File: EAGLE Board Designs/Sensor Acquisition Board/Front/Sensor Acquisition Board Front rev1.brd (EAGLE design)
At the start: 116.8 x 50.8 mm, 41 parts, among them J1 CONNECTOR-SENSOR_NF_S_RA_BLACK, J10 JUMPER_0603_, J2 CONNECTOR-SENSOR_NF_S_RA_BLACK, J3 CONNECTOR-CAN_NF_S_RA_BLACK, J4 CONNECTOR-CAN_NF_S_RA_BLACK, J6 JUMPER_0603_, U1 VOLTAGE_REGULATOR_SOT-223_5V, U2 MCP2562FD, U3 MCP2562FD

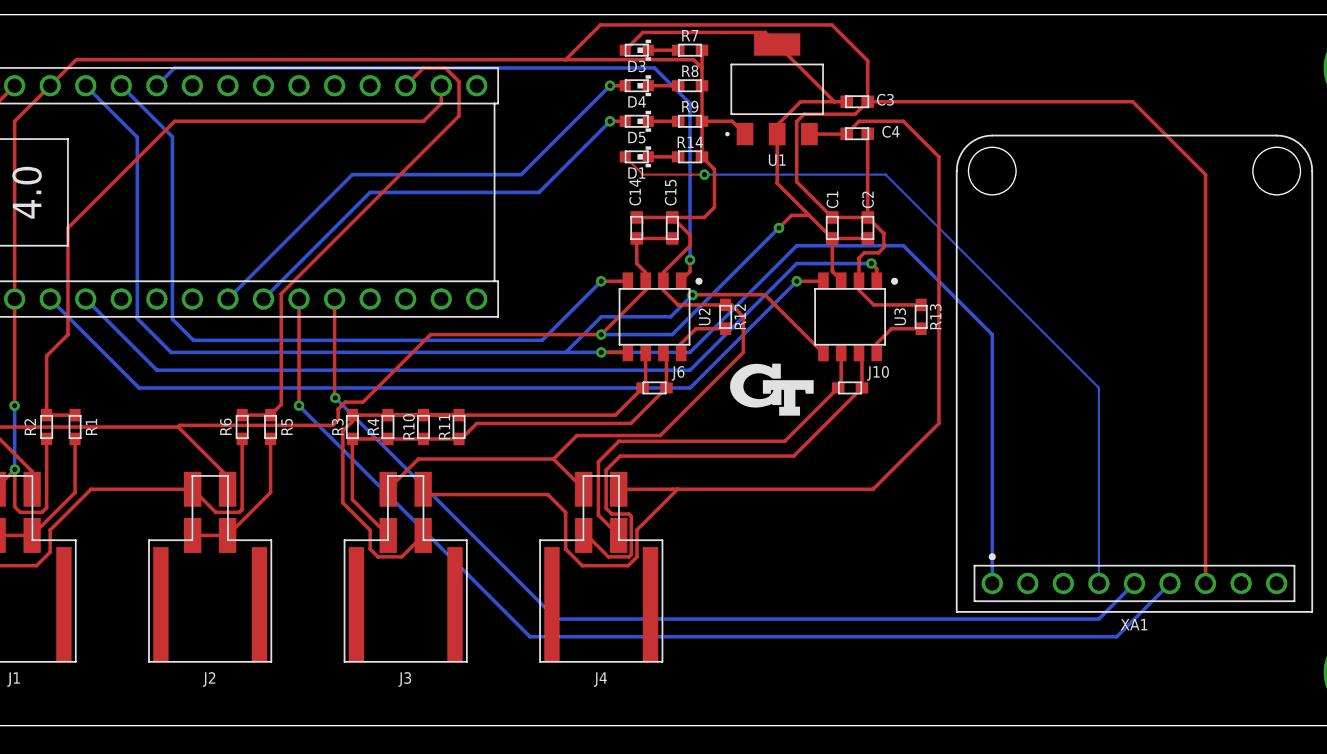
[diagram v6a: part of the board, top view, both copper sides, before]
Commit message: Fixed GPS connections
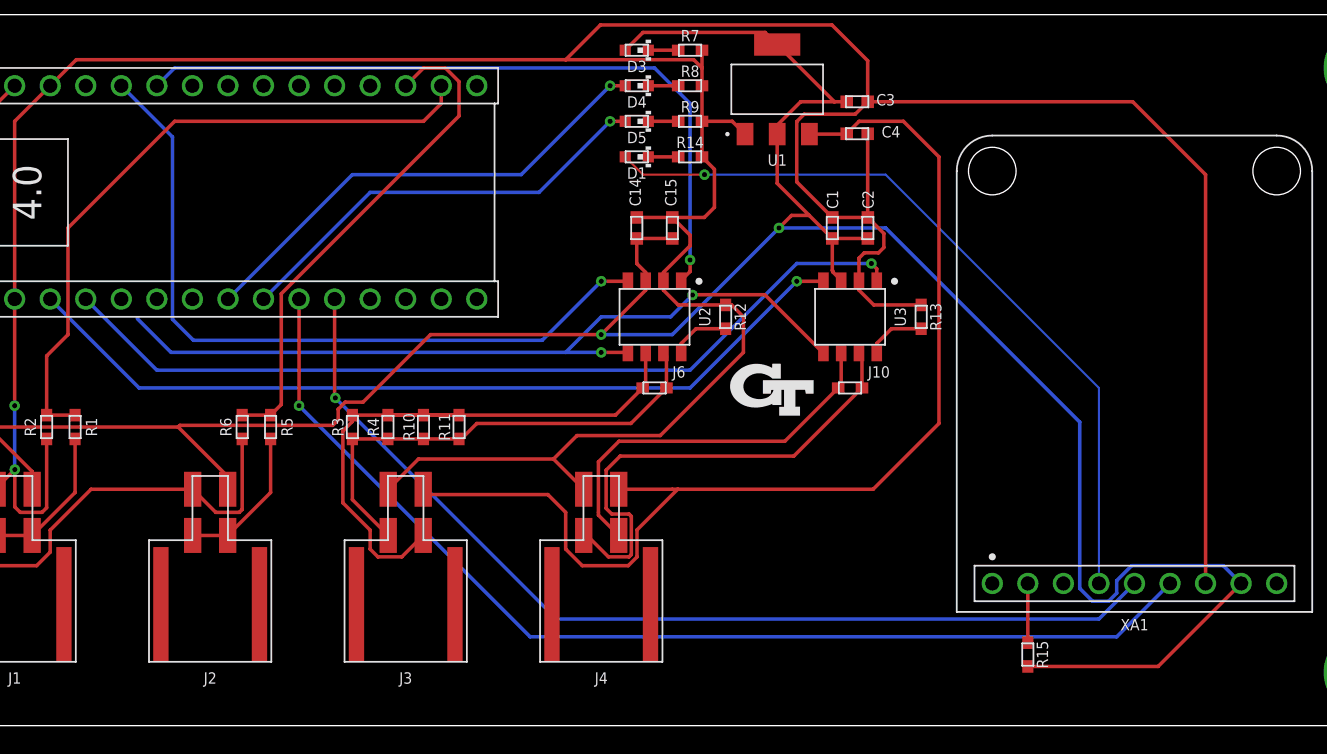
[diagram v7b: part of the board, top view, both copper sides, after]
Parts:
- added R15: RESISTOR_0603_10K, HyTechDevices:0603-RES
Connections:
- removed net VIN: XA1.VIN
- new net 3.3V: A2.3.3V
- new net 3V3: XA1.3.3V
- new net N$7: R15.1, XA1.EN
- net +5V: now also R15.2, XA1.VIN
- net TEENSY_3.3V: no longer A2.3.3V, XA1.3.3V
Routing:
- net +5V: track 152.5 -> 223.4 mm
- net TEENSY_3.3V: track 127.6 -> 57.9 mm
- net N$7: track 0.00 -> 4.23 mm
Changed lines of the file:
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@@
 <attribute name="NAME" x="60.96" y="39.89" size="0.8128" layer="25" font="vector" rot="R180" align="bottom-center"/>
+</element>
+<element name="R15" library="HyTechDevices" package="0603-RES" value="RESISTOR_0603_10K" x="88.9" y="5.08" smashed="yes" rot="R270">
+<attribute name="DKPN" value="311-10.0KHRCT-ND" x="88.9" y="5.08" size="1.778" layer="27" rot="R270" display="off"/>
+<attribute name="MANUFACTURER" value="Yageo" x="88.9" y="5.08" size="1.778" layer="27" rot="R270" display="off"/>
+<attribute name="MOPN" value="603-RC0603FR-0710KL" x="88.9" y="5.08" size="1.778" layer="27" rot="R270" display="off"/>
+<attribute name="MPN" value="RC0603FR-0710KL" x="88.9" y="5.08" size="1.778" layer="27" rot="R270" display="off"/>
+<attribute name="NAME" x="89.535" y="5.08" size="0.8128" layer="25" font="vector" rot="R270" align="bottom-center"/>
+<attribute name="POWER" value="0.1W" x="88.9" y="5.08" size="1.778" layer="27" rot="R270" display="off"/>
+<attribute name="RESISTANCE" value="10k" x="88.9" y="5.08" size="1.778" layer="27" rot="R270" display="off"/>
+<attribute name="TOLERANCE" value="1%" x="88.9" y="5.08" size="1.778" layer="27" rot="R270" display="off"/>
+<attribute name="VOLTAGE_CONTINUOUS" value="31.62V" x="88.9" y="5.08" size="1.778" layer="27" rot="R270" display="off"/>
+<attribute name="VOLTAGE_MAX" value="75V" x="88.9" y="5.08" size="1.778" layer="27" rot="R270" display="off"/>
 </element>
 </elements>
@@
 <wire x1="39.2366" y1="21.4566" x2="39.624" y2="21.844" width="0.254" layer="1"/>
 <wire x1="40.132" y1="23.114" x2="41.402" y2="23.114" width="0.254" layer="1"/>
+<contactref element="XA1" pad="VIN"/>
+<contactref element="R15" pad="2"/>
+<wire x1="88.9" y1="4.23" x2="98.21" y2="4.23" width="0.254" layer="1"/>
+<wire x1="98.21" y1="4.23" x2="104.14" y2="10.16" width="0.254" layer="1"/>
+<wire x1="104.14" y1="10.16" x2="102.87" y2="11.43" width="0.254" layer="16"/>
+<wire x1="96.3172375" y1="11.43" x2="95.25" y2="10.3627625" width="0.254" layer="16"/>
+<wire x1="95.25" y1="10.3627625" x2="95.25" y2="9.4647375" width="0.254" layer="16"/>
+<wire x1="93.5232375" y1="8.89" x2="92.6084" y2="9.8048375" width="0.254" layer="16"/>
+<wire x1="78.74" y1="35.56" x2="71.12" y2="35.56" width="0.254" layer="16"/>
+<wire x1="102.87" y1="11.43" x2="96.3172375" y2="11.43" width="0.254" layer="16"/>
+<wire x1="95.25" y1="9.4647375" x2="94.6752625" y2="8.89" width="0.254" layer="16"/>
+<wire x1="94.6752625" y1="8.89" x2="93.5232375" y2="8.89" width="0.254" layer="16"/>
+<wire x1="92.6084" y1="9.8048375" x2="92.6084" y2="21.6916" width="0.254" layer="16"/>
+<wire x1="92.6084" y1="21.6916" x2="78.74" y2="35.56" width="0.254" layer="16"/>
 </signal>
 <signal name="+12V">
@@
 </signal>
 <signal name="TEENSY_3.3V">
-<contactref element="A2" pad="3.3V"/>
 <contactref element="U2" pad="5"/>
 <contactref element="U3" pad="5"/>
-<wire x1="21.59" y1="45.72" x2="25.273" y2="42.037" width="0.254" layer="16"/>
-<wire x1="25.273" y1="42.037" x2="25.273" y2="29.083" width="0.254" layer="16"/>
 <wire x1="25.273" y1="29.083" x2="27.686" y2="26.67" width="0.254" layer="16"/>
 <wire x1="27.686" y1="26.67" x2="55.88" y2="26.67" width="0.254" layer="16"/>
@@
 <wire x1="70.1121" y1="30.7894" x2="64.961425" y2="30.7894" width="0.254" layer="1"/>
 <wire x1="58.42" y1="29.21" x2="55.88" y2="26.67" width="0.254" layer="16"/>
-<contactref element="XA1" pad="3.3V"/>
-<wire x1="58.42" y1="26.67" x2="64.77" y2="26.67" width="0.254" layer="16"/>
-<wire x1="64.77" y1="26.67" x2="72.39" y2="34.29" width="0.254" layer="16"/>
-<wire x1="72.39" y1="34.29" x2="80.01" y2="34.29" width="0.254" layer="16"/>
-<wire x1="86.36" y1="27.94" x2="86.36" y2="10.16" width="0.254" layer="16"/>
-<wire x1="80.01" y1="34.29" x2="86.36" y2="27.94" width="0.254" layer="16"/>
 </signal>
 <signal name="SENSOR_1">
@@
 <wire x1="78.105" y1="27.305" x2="79.16" y2="28.36" width="0.254" layer="1"/>
 </signal>
-<signal name="VIN">
-<contactref element="XA1" pad="VIN"/>
-</signal>
 <signal name="VBAT">
 <contactref element="XA1" pad="VBAT"/>
@@
 <wire x1="78.74" y1="39.37" x2="65.7978" y2="39.37" width="0.1524" layer="16"/>
 </signal>
+<signal name="N$7">
+<contactref element="XA1" pad="EN"/>
+<contactref element="R15" pad="1"/>
+<wire x1="88.9" y1="10.16" x2="88.9" y2="5.93" width="0.254" layer="1"/>
+</signal>
+<signal name="3V3">
+<contactref element="XA1" pad="3.3V"/>
+</signal>
+<signal name="3.3V">
+<contactref element="A2" pad="3.3V"/>
+</signal>
 </signals>

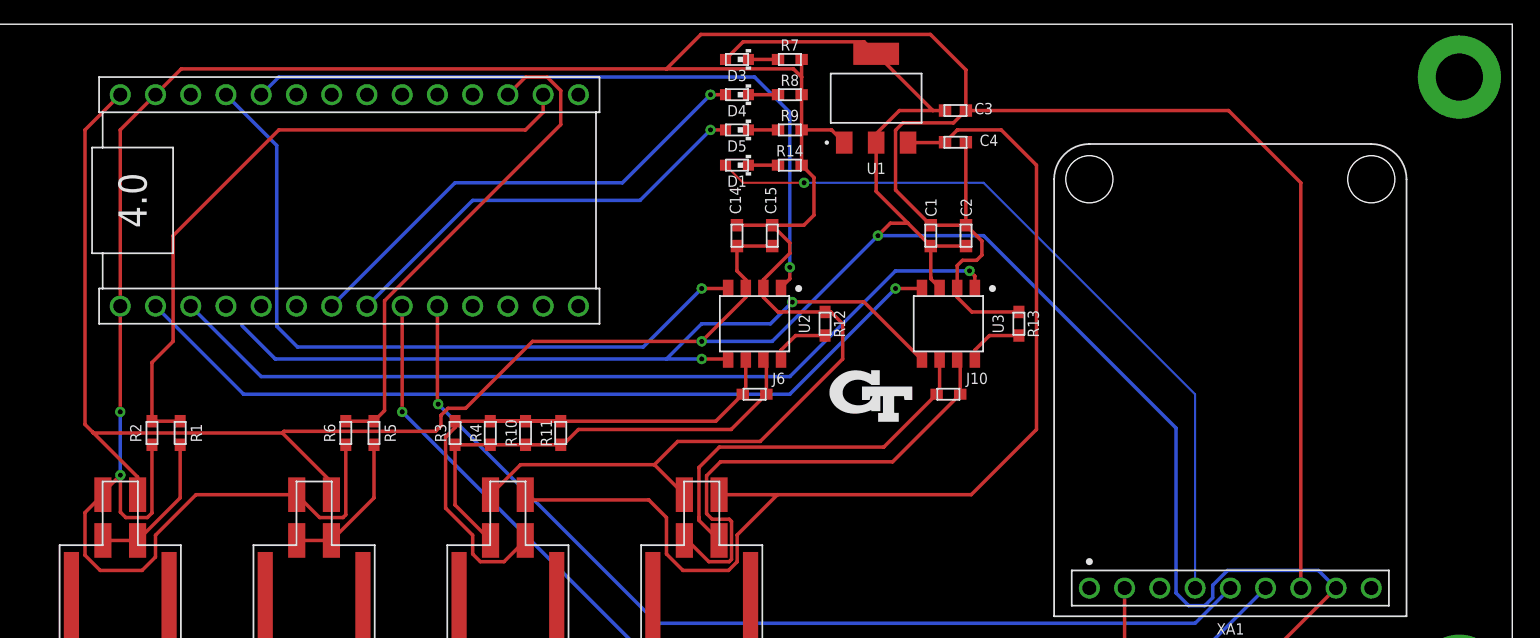
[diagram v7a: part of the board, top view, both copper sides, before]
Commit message: Fixed solder mask
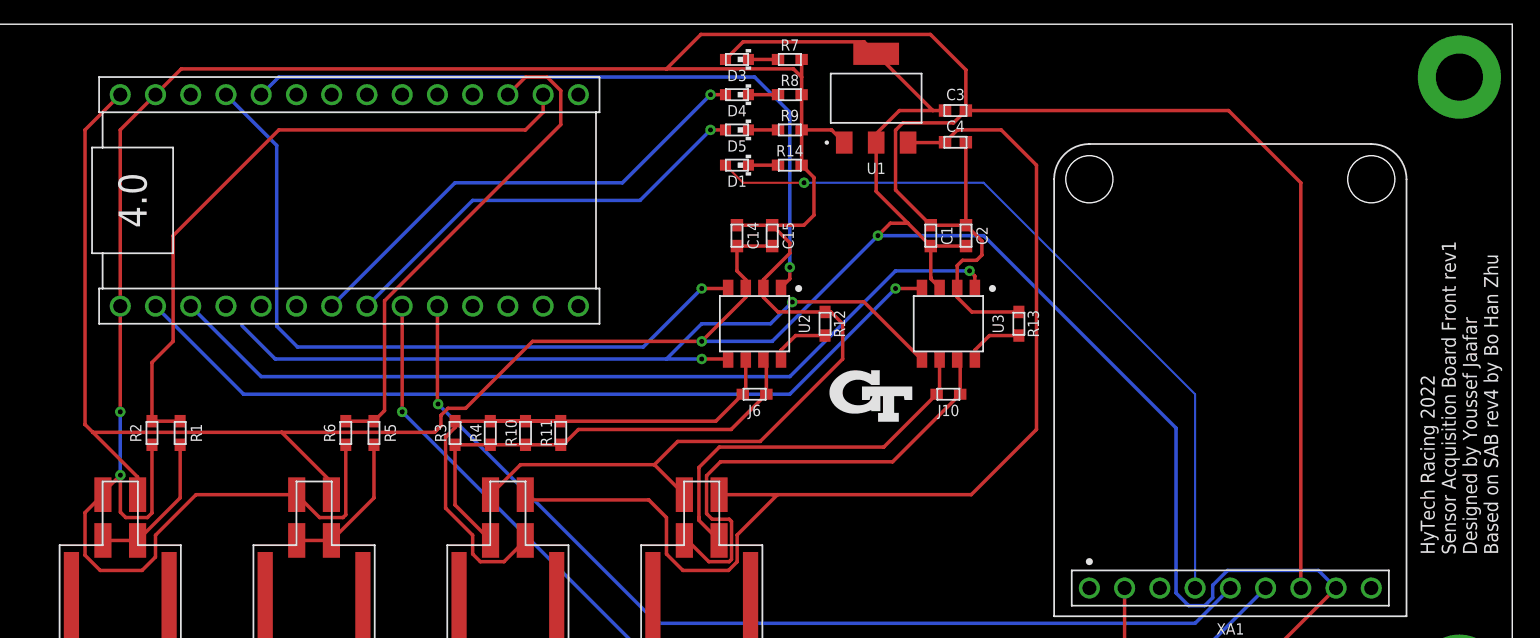
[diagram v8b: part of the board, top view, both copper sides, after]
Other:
- board text added: "HyTech Racing 2022 Sensor Acquisition Board Front rev1 Designed by Youssef Jaafar Based on SAB rev4 by Bo Han Zhu"
- board text removed: "HyTech Racing 2022 Sensor Acquisition Board Front rev1 Designed by Bo Han Zhu"
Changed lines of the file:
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@@
 <drawing>
 <settings>
-<setting alwaysvectorfont="no"/>
+<setting alwaysvectorfont="yes"/>
 <setting verticaltext="up"/>
 </settings>
@@
 <wire x1="116.84" y1="50.8" x2="0" y2="50.8" width="0" layer="20"/>
 <wire x1="0" y1="50.8" x2="0" y2="0" width="0" layer="20"/>
-<text x="114.554" y="12.573" size="1.016" layer="51" font="vector" rot="R90">HyTech Racing 2022
+<text x="115.824" y="12.573" size="1.016" layer="21" font="vector" rot="R90">HyTech Racing 2022
 Sensor Acquisition Board Front rev1
-Designed by Bo Han Zhu</text>
+Designed by Youssef Jaafar
+Based on SAB rev4 by Bo Han Zhu</text>
 <text x="52.578" y="3.175" size="0.8128" layer="51" rot="R90">Vehicle CAN-Bus</text>
 <text x="10.668" y="3.175" size="0.8128" layer="51" rot="R90">1. F-L Suspension Linear Pot</text>
@@
 <attribute name="MOPN" value="77-VJ0603Y104JXQPBC" x="8.89" y="-11.43" size="1.778" layer="27" rot="R270" display="off"/>
 <attribute name="MPN" value="VJ0603Y104JXQPW1BC" x="8.89" y="-11.43" size="1.778" layer="27" rot="R270" display="off"/>
-<attribute name="NAME" x="74.537" y="37.592" size="0.8128" layer="25" font="vector" rot="R270" align="bottom-center"/>
+<attribute name="NAME" x="75.68" y="35.56" size="0.8128" layer="25" font="vector" rot="R270" align="bottom-center"/>
 <attribute name="TOLERANCE" value="5%" x="8.89" y="-11.43" size="1.778" layer="27" rot="R270" display="off"/>
 <attribute name="VOLTAGE" value="10V" x="8.89" y="-11.43" size="1.778" layer="27" rot="R270" display="off"/>
@@
 <attribute name="MOPN" value="187-CL10B105KA8NNNC" x="135.128" y="-23.749" size="1.778" layer="27" display="off"/>
 <attribute name="MPN" value="CL10B105KA8NNNC" x="135.128" y="-23.749" size="1.778" layer="27" display="off"/>
-<attribute name="NAME" x="79.121" y="42.025" size="0.8128" layer="25" font="vector" align="bottom-center"/>
+<attribute name="NAME" x="76.708" y="43.041" size="0.8128" layer="25" font="vector" align="bottom-center"/>
 <attribute name="TOLERANCE" value="10%" x="135.128" y="-23.749" size="1.778" layer="27" display="off"/>
 <attribute name="VOLTAGE" value="25V" x="135.128" y="-23.749" size="1.778" layer="27" display="off"/>
@@
 <attribute name="MOPN" value="187-CL10A475KP8NNNC" x="127.508" y="-21.463" size="1.778" layer="27" display="off"/>
 <attribute name="MPN" value="CL10A475KP8NNNC" x="127.508" y="-21.463" size="1.778" layer="27" display="off"/>
-<attribute name="NAME" x="78.74" y="44.311" size="0.8128" layer="25" font="vector" align="bottom-center"/>
+<attribute name="NAME" x="76.708" y="45.327" size="0.8128" layer="25" font="vector" align="bottom-center"/>
 <attribute name="TOLERANCE" value="10%" x="127.508" y="-21.463" size="1.778" layer="27" display="off"/>
 <attribute name="VOLTAGE" value="10V" x="127.508" y="-21.463" size="1.778" layer="27" display="off"/>
@@
 <attribute name="MOPN" value="603-CC603KRX7R6BB105" x="11.43" y="-19.05" size="1.778" layer="27" rot="R270" display="off"/>
 <attribute name="MPN" value="CC0603KRX7R6BB105" x="11.43" y="-19.05" size="1.778" layer="27" rot="R270" display="off"/>
-<attribute name="NAME" x="77.077" y="37.592" size="0.8128" layer="25" font="vector" rot="R270" align="bottom-center"/>
+<attribute name="NAME" x="78.22" y="35.56" size="0.8128" layer="25" font="vector" rot="R270" align="bottom-center"/>
 <attribute name="TOLERANCE" value="10%" x="11.43" y="-19.05" size="1.778" layer="27" rot="R270" display="off"/>
 <attribute name="VOLTAGE" value="10V" x="11.43" y="-19.05" size="1.778" layer="27" rot="R270" display="off"/>
@@
 <attribute name="MOPN" value="603-RC0603FR-130RL" x="76.2" y="24.13" size="1.778" layer="27" rot="R180" display="off"/>
 <attribute name="MPN" value="RC0603FR-130RL" x="76.2" y="24.13" size="1.778" layer="27" rot="R180" display="off"/>
-<attribute name="NAME" x="77.47" y="25.273" size="0.8128" layer="25" font="vector" rot="R180" align="center-right"/>
+<attribute name="NAME" x="76.2" y="23.368" size="0.8128" layer="25" font="vector" rot="R180" align="bottom-center"/>
 </element>
 <element name="J2" library="HyTechDevices" package="MOLEX_NANOFIT_SMD_RIGHTANGLE_04" value="CONNECTOR-SENSOR_NF_S_RA_BLACK" x="30.48" y="15.24" smashed="yes">
@@
 <attribute name="MOPN" value="77-VJ0603Y104JXQPBC" x="90.17" y="88.9" size="1.778" layer="27" rot="R270" display="off"/>
 <attribute name="MPN" value="VJ0603Y104JXQPW1BC" x="90.17" y="88.9" size="1.778" layer="27" rot="R270" display="off"/>
-<attribute name="NAME" x="62.98" y="38.1" size="0.8128" layer="25" font="vector" rot="R270" align="bottom-center"/>
+<attribute name="NAME" x="64.25" y="35.56" size="0.8128" layer="25" font="vector" rot="R270" align="bottom-center"/>
 <attribute name="TOLERANCE" value="5%" x="90.17" y="88.9" size="1.778" layer="27" rot="R270" display="off"/>
 <attribute name="VOLTAGE" value="10V" x="90.17" y="88.9" size="1.778" layer="27" rot="R270" display="off"/>
@@
 <attribute name="MOPN" value="603-CC603KRX7R6BB105" x="83.82" y="85.09" size="1.778" layer="27" rot="R270" display="off"/>
 <attribute name="MPN" value="CC0603KRX7R6BB105" x="83.82" y="85.09" size="1.778" layer="27" rot="R270" display="off"/>
-<attribute name="NAME" x="60.44" y="38.1" size="0.8128" layer="25" font="vector" rot="R270" align="bottom-center"/>
+<attribute name="NAME" x="61.71" y="35.56" size="0.8128" layer="25" font="vector" rot="R270" align="bottom-center"/>
 <attribute name="TOLERANCE" value="10%" x="83.82" y="85.09" size="1.778" layer="27" rot="R270" display="off"/>
 <attribute name="VOLTAGE" value="10V" x="83.82" y="85.09" size="1.778" layer="27" rot="R270" display="off"/>
@@
 <attribute name="MOPN" value="603-RC0603FR-130RL" x="62.23" y="24.13" size="1.778" layer="27" rot="R180" display="off"/>
 <attribute name="MPN" value="RC0603FR-130RL" x="62.23" y="24.13" size="1.778" layer="27" rot="R180" display="off"/>
-<attribute name="NAME" x="63.5" y="25.273" size="0.8128" layer="25" font="vector" rot="R180" align="center-right"/>
+<attribute name="NAME" x="62.23" y="23.368" size="0.8128" layer="25" font="vector" rot="R180" align="bottom-center"/>
 </element>
 <element name="R7" library="HyTechDevices" package="0603-RES" value="RESISTOR_0603_1K" x="64.77" y="48.26" smashed="yes">
@@
 <wire x1="16.51" y1="45.72" x2="13.97" y2="43.18" width="0.254" layer="1"/>
 <wire x1="17.76" y1="18.16" x2="17.76" y2="16.89" width="0.254" layer="1"/>
-<wire x1="17.76" y1="18.16" x2="14.531" y2="21.389" width="0.254" layer="1"/>
-<wire x1="14.531" y1="21.389" x2="13.97" y2="21.95" width="0.254" layer="1"/>
-<wire x1="13.97" y1="43.18" x2="13.97" y2="21.95" width="0.254" layer="1"/>
-<wire x1="14.583996875" y1="21.336" x2="14.531" y2="21.389" width="0.254" layer="1"/>
+<wire x1="17.76" y1="18.16" x2="14.53526875" y2="21.384734375" width="0.254" layer="1"/>
+<wire x1="13.97" y1="21.95" x2="13.97" y2="43.18" width="0.254" layer="1"/>
 <wire x1="31.73" y1="16.89" x2="31.73" y2="17.8" width="0.254" layer="1"/>
-<wire x1="31.73" y1="17.8" x2="28.194" y2="21.336" width="0.254" layer="1"/>
-<wire x1="28.194" y1="21.336" x2="14.583996875" y2="21.336" width="0.254" layer="1"/>
 <wire x1="60.96" y1="34.81" x2="63.5" y2="34.81" width="0.254" layer="1"/>
 <wire x1="60.96" y1="33.02" x2="60.96" y2="34.81" width="0.254" layer="1"/>
@@
 <wire x1="70.129" y1="49.53" x2="70.993" y2="48.666" width="0.254" layer="1"/>
 <wire x1="70.993" y1="48.666" x2="75.082" y2="44.577" width="0.254" layer="1"/>
-<wire x1="28.194" y1="21.336" x2="28.3146" y2="21.4566" width="0.254" layer="1"/>
 <wire x1="46.228" y1="27.94" x2="58.42" y2="27.94" width="0.254" layer="1"/>
 <wire x1="39.624" y1="21.844" x2="39.624" y2="22.606" width="0.254" layer="1"/>
 <wire x1="39.624" y1="22.606" x2="40.132" y2="23.114" width="0.254" layer="1"/>
 <wire x1="41.402" y1="23.114" x2="46.228" y2="27.94" width="0.254" layer="1"/>
-<wire x1="28.3146" y1="21.4566" x2="39.2366" y2="21.4566" width="0.254" layer="1"/>
-<wire x1="39.2366" y1="21.4566" x2="39.624" y2="21.844" width="0.254" layer="1"/>
+<wire x1="39.2366" y1="21.4566" x2="39.37" y2="21.59" width="0.254" layer="1"/>
+<wire x1="39.37" y1="21.59" x2="39.624" y2="21.844" width="0.254" layer="1"/>
 <wire x1="40.132" y1="23.114" x2="41.402" y2="23.114" width="0.254" layer="1"/>
 <contactref element="XA1" pad="VIN"/>
@@
 <wire x1="92.6084" y1="9.8048375" x2="92.6084" y2="21.6916" width="0.254" layer="16"/>
 <wire x1="92.6084" y1="21.6916" x2="78.74" y2="35.56" width="0.254" layer="16"/>
+<wire x1="14.53526875" y1="21.384734375" x2="13.970003125" y2="21.95" width="0.254" layer="1"/>
+<wire x1="13.970003125" y1="21.95" x2="13.97" y2="21.95" width="0.254" layer="1"/>
+<wire x1="28.145265625" y1="21.384734375" x2="14.53526875" y2="21.384734375" width="0.254" layer="1"/>
+<wire x1="31.73" y1="17.8" x2="28.145265625" y2="21.384734375" width="0.254" layer="1"/>
+<wire x1="39.2366" y1="21.4566" x2="39.164734375" y2="21.384734375" width="0.254" layer="1"/>
+<wire x1="39.164734375" y1="21.384734375" x2="28.145265625" y2="21.384734375" width="0.254" layer="1"/>
 </signal>
 <signal name="+12V">
